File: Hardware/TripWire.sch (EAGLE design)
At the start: 67 parts, among them P1 LSP11, P2 LSP11, P3 LSP11, P4 LSP11, P5 LSP11, P6 LSP11, P7 LSP11, X1 GADGETEER-SOCKET

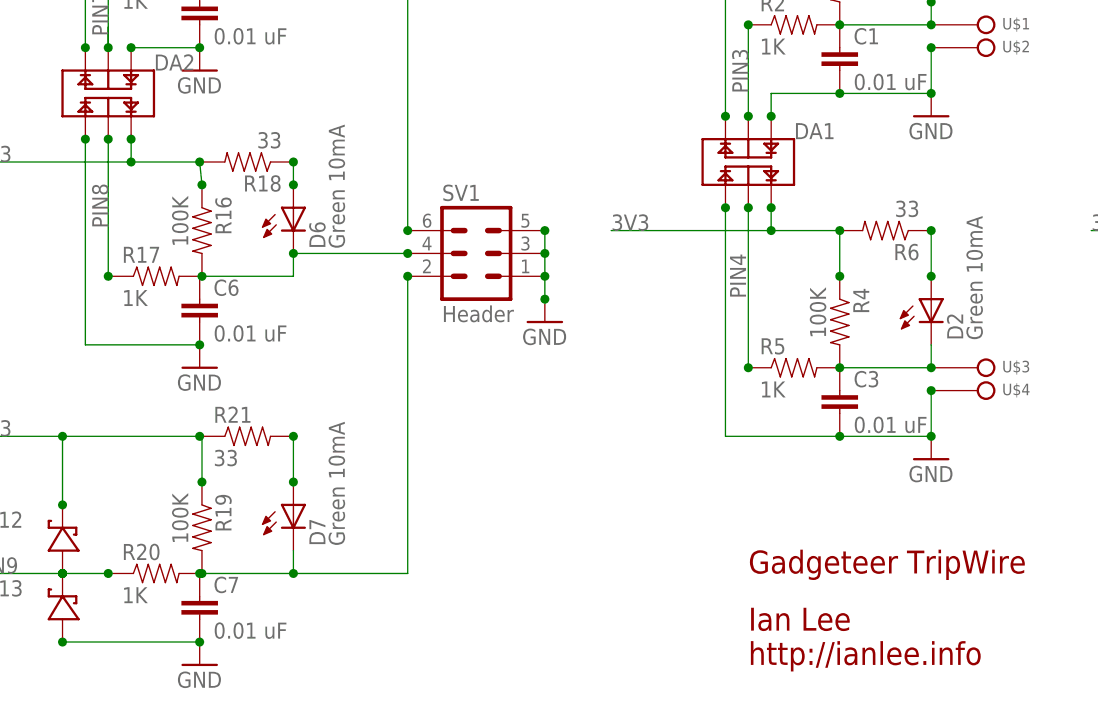
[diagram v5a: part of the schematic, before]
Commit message: Optimized some routes.
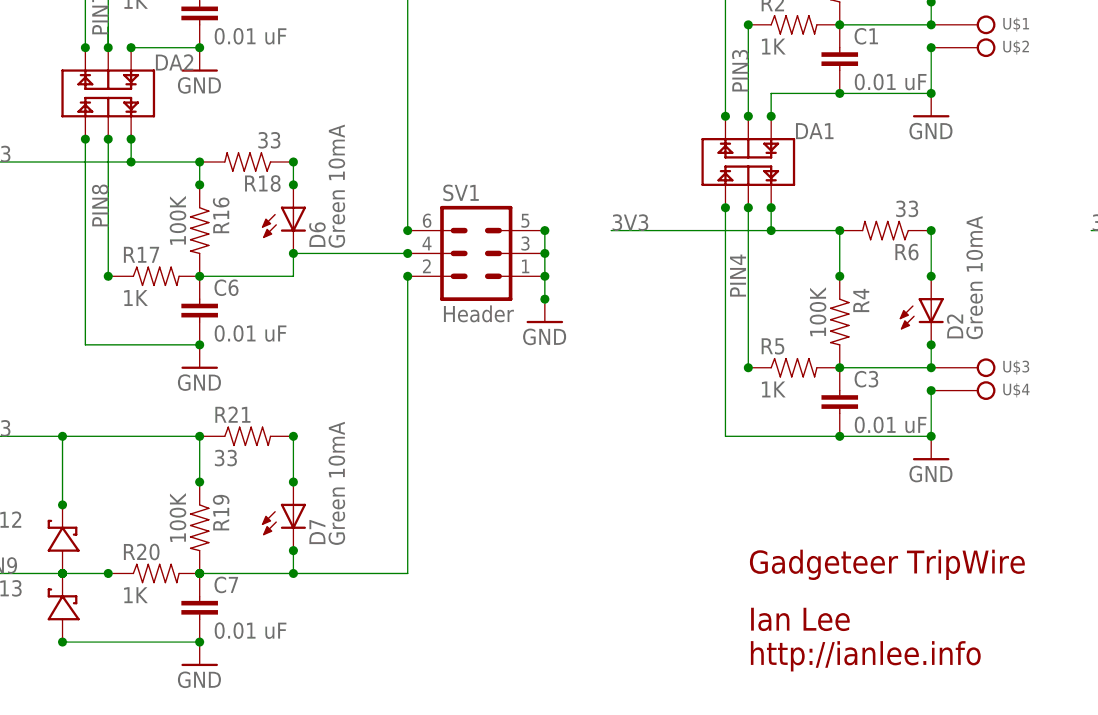
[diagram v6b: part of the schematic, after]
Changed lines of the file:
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@@
 <instance part="R15" gate="G$1" x="38.354" y="99.06"/>
 <instance part="D6" gate="G$1" x="43.434" y="58.42"/>
-<instance part="R16" gate="G$1" x="33.274" y="55.88" rot="R270"/>
+<instance part="R16" gate="G$1" x="33.02" y="55.88" rot="R270"/>
 <instance part="R17" gate="G$1" x="28.194" y="50.8"/>
 <instance part="R18" gate="G$1" x="38.354" y="63.5" rot="R180"/>
 <instance part="D7" gate="G$1" x="43.434" y="25.4"/>
-<instance part="R19" gate="G$1" x="33.274" y="22.86" rot="R270"/>
+<instance part="R19" gate="G$1" x="33.02" y="22.86" rot="R270"/>
 <instance part="R20" gate="G$1" x="28.194" y="17.78"/>
 <instance part="R21" gate="G$1" x="38.354" y="33.02"/>
@@
 <segment>
 <pinref part="R19" gate="G$1" pin="1"/>
-<wire x1="33.274" y1="27.94" x2="33.274" y2="33.02" width="0.1524" layer="91"/>
-<junction x="33.274" y="27.94"/>
+<wire x1="33.02" y1="27.94" x2="33.02" y2="33.02" width="0.1524" layer="91"/>
+<junction x="33.02" y="27.94"/>
 </segment>
 <segment>
@@
 <wire x1="33.02" y1="63.5" x2="25.4" y2="63.5" width="0.1524" layer="91"/>
 <wire x1="25.4" y1="63.5" x2="7.874" y2="63.5" width="0.1524" layer="91"/>
-<wire x1="33.274" y1="60.96" x2="33.02" y2="63.5" width="0.1524" layer="91"/>
+<wire x1="33.02" y1="60.96" x2="33.02" y2="63.5" width="0.1524" layer="91"/>
 <junction x="33.02" y="63.5"/>
 <wire x1="25.4" y1="66.04" x2="25.4" y2="63.5" width="0.1524" layer="91"/>
@@
 <junction x="25.4" y="66.04"/>
 <pinref part="R16" gate="G$1" pin="1"/>
-<junction x="33.274" y="60.96"/>
+<junction x="33.02" y="60.96"/>
 </segment>
 <segment>
@@
 <pinref part="R16" gate="G$1" pin="2"/>
 <pinref part="R17" gate="G$1" pin="2"/>
-<junction x="33.274" y="50.8"/>
-<wire x1="33.274" y1="50.8" x2="33.02" y2="50.8" width="0.1524" layer="91"/>
+<junction x="33.02" y="50.8"/>
 <pinref part="C6" gate="G$1" pin="1"/>
 <wire x1="33.02" y1="50.8" x2="43.434" y2="50.8" width="0.1524" layer="91"/>
 <wire x1="43.434" y1="50.8" x2="43.434" y2="53.34" width="0.1524" layer="91"/>
 <junction x="43.434" y="53.34"/>
+<wire x1="33.02" y1="50.8" x2="33.274" y2="50.8" width="0.1524" layer="91"/>
 </segment>
 </net>
@@
 <junction x="104.14" y="40.64"/>
 <pinref part="C3" gate="G$1" pin="1"/>
+<junction x="114.3" y="43.18"/>
 </segment>
 </net>
@@
 <pinref part="R20" gate="G$1" pin="2"/>
 <pinref part="SV1" gate="1" pin="2"/>
-<wire x1="33.274" y1="17.78" x2="33.02" y2="17.78" width="0.1524" layer="91"/>
 <wire x1="33.02" y1="17.78" x2="43.434" y2="17.78" width="0.1524" layer="91"/>
 <wire x1="43.434" y1="17.78" x2="56.134" y2="17.78" width="0.1524" layer="91"/>
@@
 <wire x1="43.434" y1="20.32" x2="43.434" y2="17.78" width="0.1524" layer="91"/>
 <junction x="43.434" y="17.78"/>
-<junction x="33.274" y="17.78"/>
+<junction x="33.02" y="17.78"/>
 <junction x="56.134" y="50.8"/>
 <pinref part="C7" gate="G$1" pin="1"/>
 <junction x="33.02" y="17.78"/>
-</segment>
-</net>
+<wire x1="33.02" y1="17.78" x2="33.274" y2="17.78" width="0.1524" layer="91"/>
+<junction x="43.434" y="20.32"/>
+</segment>
+</net>
